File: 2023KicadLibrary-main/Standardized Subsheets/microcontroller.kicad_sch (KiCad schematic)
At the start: 57 parts, among them J3 Conn_01x02, J4 Conn_01x02, J5 SWD, SW1 SW_SPDT, U2 STM32F105RCTx, U3 SN65HVD230, U4 SN65HVD230, Y1 16MHz

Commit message: with layout
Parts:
- renumbered D1 to D7, D2 to D8, D3 to D9, J3 to J6, J4 to J7, J5 to J8, R4 to R13, R5 to R14, R6 to R15, R7 to R16, R8 to R17, R9 to R18, R10 to R19, R11 to R20, R12 to R21, R13 to R22, R14 to R23, R15 to R24, R16 to R25, R17 to R26, R18 to R27, R19 to R28, R20 to R29, R21 to R30, R22 to R31, SW1 to SW3, TP8 to TP10, TP1 to TP3, TP2 to TP4, TP3 to TP5, TP4 to TP6, TP5 to TP7, TP6 to TP8, TP7 to TP9

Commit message: new HUD PCB
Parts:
- D8: footprint Global Libraries:SOT95P280X100-6N -> Global Libraries_2:SOT95P280X100-6N
- renumbered JP1 to JP5, JP2 to JP6, JP3 to JP7, JP4 to JP8, TP6 to TP10, TP7 to TP11, TP8 to TP12, TP9 to TP13, TP10 to TP14, TP3 to TP7, TP4 to TP8, TP5 to TP9
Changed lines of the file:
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@@
   (symbol (lib_id "Jumper:Jumper_2_Bridged") (at 191.77 144.78 0) (unit 1)
     (in_bom yes) (on_board yes)
-    (property "Reference" "JP3" (id 0) (at 191.77 142.24 0))
+    (property "Reference" "JP7" (id 0) (at 191.77 142.24 0))
     (property "Value" " " (id 1) (at 191.77 142.9821 0))
     (property "Footprint" "Jumper:SolderJumper-2_P1.3mm_Bridged2Bar_Pad1.0x1.5mm" (id 2) (at 191.77 144.78 0)
@@
       (effects (font (size 1.27 1.27)) (justify right))
     )
-    (property "Footprint" "Global Libraries:SOT95P280X100-6N" (id 2) (at 119.38 115.57 0)
+    (property "Footprint" "Global Libraries_2:SOT95P280X100-6N" (id 2) (at 119.38 115.57 0)
       (effects (font (size 1.27 1.27)) (justify left) hide)
     )
@@
   (symbol (lib_id "Connector:TestPoint") (at 181.61 101.6 0) (unit 1)
     (in_bom yes) (on_board yes)
-    (property "Reference" "TP7" (id 0) (at 180.34 96.52 0)
+    (property "Reference" "TP11" (id 0) (at 180.34 96.52 0)
       (effects (font (size 1.27 1.27)) (justify left))
     )
@@
   (symbol (lib_id "Connector:TestPoint") (at 104.14 97.79 0) (unit 1)
     (in_bom yes) (on_board yes)
-    (property "Reference" "TP5" (id 0) (at 102.235 92.71 0)
+    (property "Reference" "TP9" (id 0) (at 102.235 92.71 0)
       (effects (font (size 1.27 1.27)) (justify left))
     )
@@
   (symbol (lib_id "Connector:TestPoint") (at 185.42 101.6 0) (unit 1)
     (in_bom yes) (on_board yes)
-    (property "Reference" "TP9" (id 0) (at 185.42 96.52 0))
+    (property "Reference" "TP13" (id 0) (at 185.42 96.52 0))
     (property "Value" " " (id 1) (at 185.42 96.52 0))
     (property "Footprint" "TestPoint:TestPoint_THTPad_1.0x1.0mm_Drill0.5mm" (id 2) (at 190.5 101.6 0)
@@
   (symbol (lib_id "Jumper:Jumper_2_Bridged") (at 191.77 147.32 0) (unit 1)
     (in_bom yes) (on_board yes)
-    (property "Reference" "JP4" (id 0) (at 191.77 149.225 0))
+    (property "Reference" "JP8" (id 0) (at 191.77 149.225 0))
     (property "Value" " " (id 1) (at 191.77 145.5221 0))
     (property "Footprint" "Jumper:SolderJumper-2_P1.3mm_Bridged2Bar_Pad1.0x1.5mm" (id 2) (at 191.77 147.32 0)
@@
   (symbol (lib_id "Connector:TestPoint") (at 181.61 143.51 0) (unit 1)
     (in_bom yes) (on_board yes)
-    (property "Reference" "TP8" (id 0) (at 180.34 138.43 0)
+    (property "Reference" "TP12" (id 0) (at 180.34 138.43 0)
       (effects (font (size 1.27 1.27)) (justify left))
     )
@@
   (symbol (lib_id "Jumper:Jumper_2_Bridged") (at 191.77 102.87 0) (unit 1)
     (in_bom yes) (on_board yes)
-    (property "Reference" "JP1" (id 0) (at 191.77 100.33 0))
+    (property "Reference" "JP5" (id 0) (at 191.77 100.33 0))
     (property "Value" " " (id 1) (at 191.77 101.0721 0))
     (property "Footprint" "Jumper:SolderJumper-2_P1.3mm_Bridged2Bar_Pad1.0x1.5mm" (id 2) (at 191.77 102.87 0)
@@
   (symbol (lib_id "Connector:TestPoint") (at 100.33 97.79 0) (unit 1)
     (in_bom yes) (on_board yes)
-    (property "Reference" "TP3" (id 0) (at 98.425 92.71 0)
+    (property "Reference" "TP7" (id 0) (at 98.425 92.71 0)
       (effects (font (size 1.27 1.27)) (justify left))
     )
@@
   (symbol (lib_id "Connector:TestPoint") (at 100.33 139.7 0) (unit 1)
     (in_bom yes) (on_board yes)
-    (property "Reference" "TP4" (id 0) (at 98.425 134.62 0)
+    (property "Reference" "TP8" (id 0) (at 98.425 134.62 0)
       (effects (font (size 1.27 1.27)) (justify left))
     )
@@
   (symbol (lib_id "Jumper:Jumper_2_Bridged") (at 191.77 105.41 0) (unit 1)
     (in_bom yes) (on_board yes)
-    (property "Reference" "JP2" (id 0) (at 191.77 107.315 0))
+    (property "Reference" "JP6" (id 0) (at 191.77 107.315 0))
     (property "Value" " " (id 1) (at 191.77 103.6121 0))
     (property "Footprint" "Jumper:SolderJumper-2_P1.3mm_Bridged2Bar_Pad1.0x1.5mm" (id 2) (at 191.77 105.41 0)
@@
   (symbol (lib_id "Connector:TestPoint") (at 185.42 143.51 0) (unit 1)
     (in_bom yes) (on_board yes)
-    (property "Reference" "TP10" (id 0) (at 185.42 138.43 0))
+    (property "Reference" "TP14" (id 0) (at 185.42 138.43 0))
     (property "Value" " " (id 1) (at 185.42 138.43 0))
     (property "Footprint" "TestPoint:TestPoint_THTPad_1.0x1.0mm_Drill0.5mm" (id 2) (at 190.5 143.51 0)
@@
   (symbol (lib_id "Connector:TestPoint") (at 104.14 139.7 0) (unit 1)
     (in_bom yes) (on_board yes)
-    (property "Reference" "TP6" (id 0) (at 102.235 134.62 0)
-      (effects (font (size 1.27 1.27)) (justify left))
-    )
+    (property "Reference" "TP10" (id 0) (at 102.235 134.62 0)
+      (effects (font (size 1.27 1.27)) (justify left))
+    )

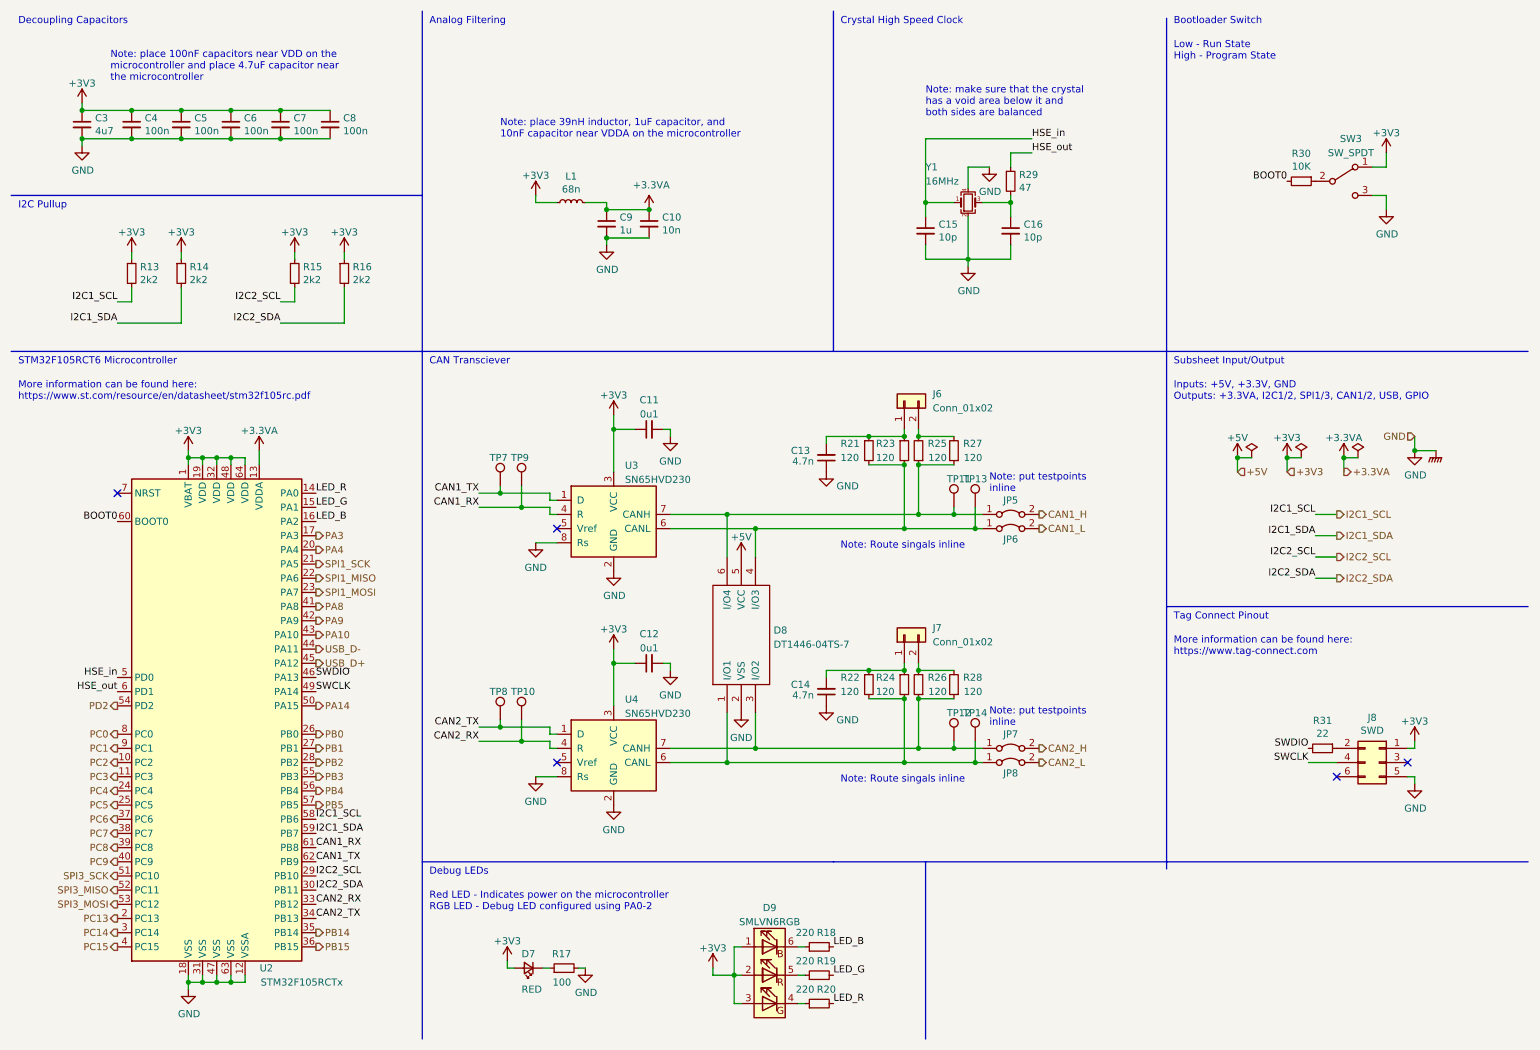
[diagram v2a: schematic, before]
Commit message: updated connector
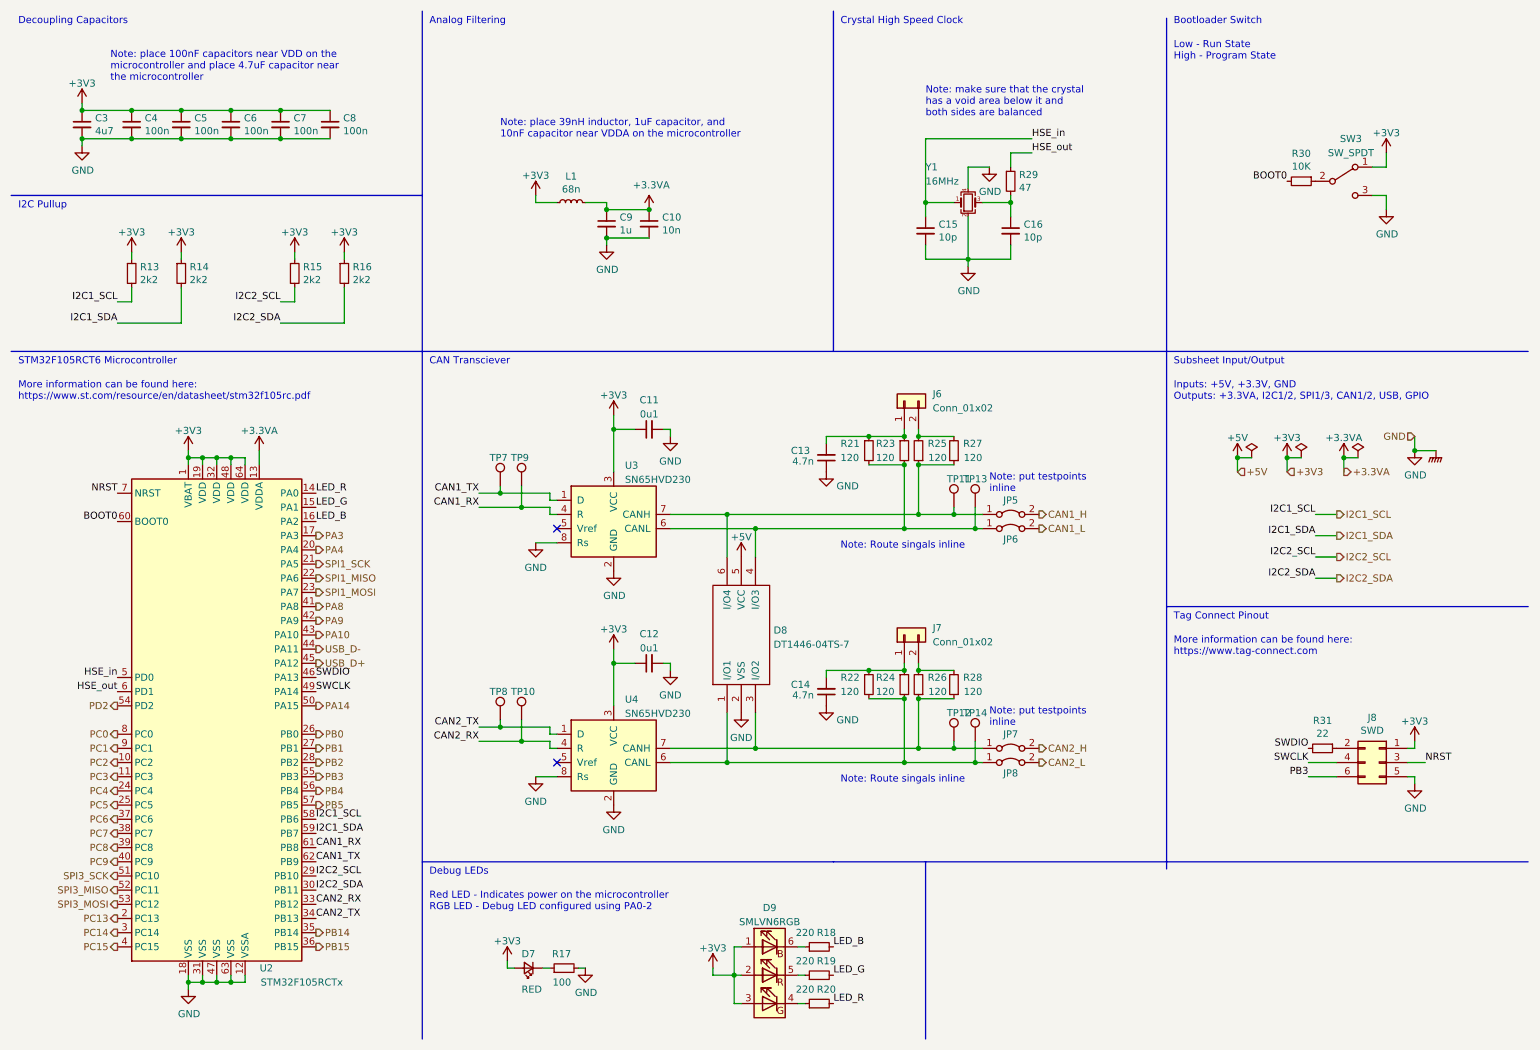
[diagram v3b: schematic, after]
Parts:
- J8: footprint Connector_PinHeader_1.27mm:PinHeader_2x03_P1.27mm_Vertical -> Connector:Tag-Connect_TC2030-IDC-FP_2x03_P1.27mm_Vertical
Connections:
- net PB3: now also J8.6 (Pin_6)
- net NRST: now reaches U2.7 (NRST)
- net NRST: now also J8.3 (Pin_3)
- no-connect marks 5 -> 2
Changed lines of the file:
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@@
   (junction (at 43.18 30.48) (diameter 0) (color 0 0 0 0)
   )
-  (no_connect (at 31.75 99.06))
-  (no_connect (at 262.89 147.32))
-  (no_connect (at 250.19 149.86))
   (no_connect (at 110.49 147.32))
   (no_connect (at 110.49 105.41))
@@
     (stroke (width 0) (type default) (color 0 0 0 0))
   )
+  (wire (pts (xy 245.11 149.86) (xy 250.19 149.86))
+    (stroke (width 0) (type default) (color 0 0 0 0))
+  )
   (wire (pts (xy 246.38 114.3) (xy 250.19 114.3))
     (stroke (width 0) (type default) (color 0 0 0 0))
@@
   )
   (wire (pts (xy 109.22 99.06) (xy 109.22 100.33))
+    (stroke (width 0) (type default) (color 0 0 0 0))
+  )
+  (wire (pts (xy 266.065 147.32) (xy 262.89 147.32))
     (stroke (width 0) (type default) (color 0 0 0 0))
   )
@@
     (effects (font (size 1.27 1.27)) (justify right bottom))
   )
+  (label "NRST" (at 31.75 99.06 180)
+    (effects (font (size 1.27 1.27)) (justify right bottom))
+  )
   (label "LED_R" (at 67.31 99.06 0)
     (effects (font (size 1.27 1.27)) (justify left bottom))
   )
+  (label "PB3" (at 245.11 149.86 180)
+    (effects (font (size 1.27 1.27)) (justify right bottom))
+  )
   (label "LED_B" (at 67.31 104.14 0)
     (effects (font (size 1.27 1.27)) (justify left bottom))
@@
   (label "CAN2_TX" (at 96.52 140.97 180)
     (effects (font (size 1.27 1.27)) (justify right bottom))
+  )
+  (label "NRST" (at 266.065 147.32 0)
+    (effects (font (size 1.27 1.27)) (justify left bottom))
   )
   (label "I2C1_SCL" (at 67.31 157.48 0)
@@
     (property "Reference" "J8" (id 0) (at 256.54 139.2682 0))
     (property "Value" "SWD" (id 1) (at 256.54 141.5796 0))
-    (property "Footprint" "Connector_PinHeader_1.27mm:PinHeader_2x03_P1.27mm_Vertical" (id 2) (at 257.81 147.32 0)
-      (effects (font (size 1.27 1.27)) hide)
-    )
+    (property "Footprint" "Connector:Tag-Connect_TC2030-IDC-FP_2x03_P1.27mm_Vertical" (id 2) (at 257.81 147.32 0)
+      (effects (font (size 1.27 1.27)) hide)
+    )
